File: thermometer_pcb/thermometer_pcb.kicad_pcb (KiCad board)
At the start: 2 copper layers, 76.6 x 49 mm, 23 parts, among them J1 POWER_IN, J2 TC_IN, J3 EXT_DS1, J4 EXT_DS2, J5 DISP, J6 Conn_01x02, J7 SPI, J8 I2C, J9 ENC, Q1 PN2222A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

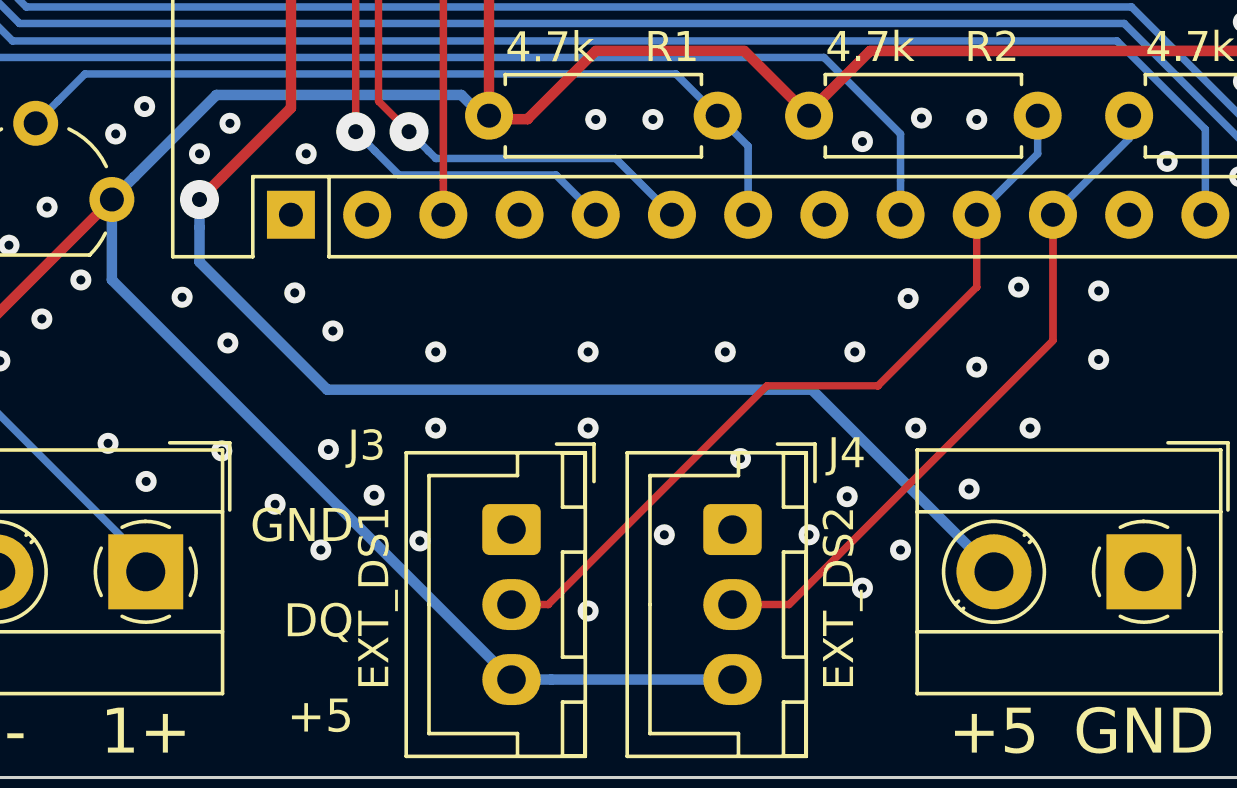
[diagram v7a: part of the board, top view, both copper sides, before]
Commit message: pcb: get rid of via on Vin track
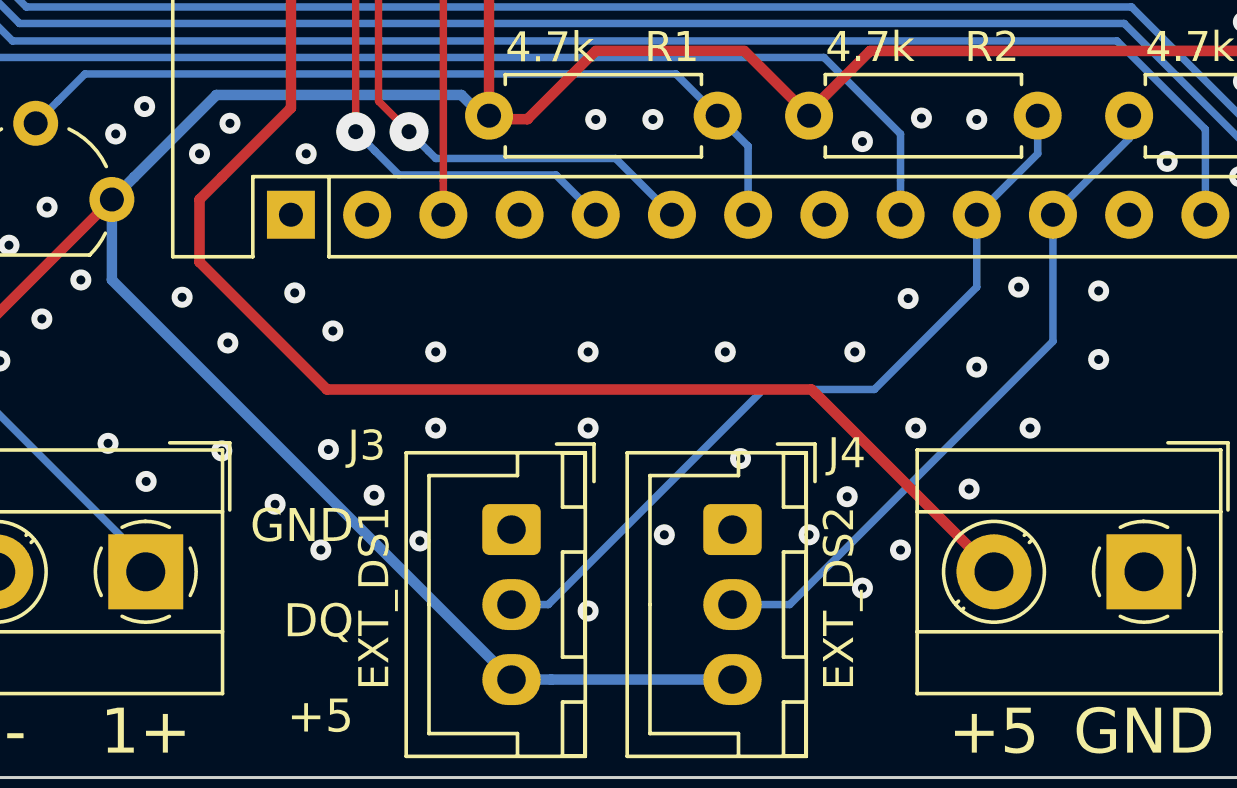
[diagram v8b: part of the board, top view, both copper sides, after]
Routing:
- net /Vin: vias 1 -> 0
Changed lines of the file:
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@@
   (gr_line (start 222.221676 76.190177) (end 222.221676 46.018604) (layer "Edge.Cuts") (width 0.1))
   (gr_arc (start 220.221676 46.018604) (end 222.221676 46.018604) (angle -90) (layer "Edge.Cuts") (width 0.1))
+  (segment (start 202.155677 80.082604) (end 205.568677 76.669604) (width 0.25) (layer "B.Cu") (net 20))
+  (segment (start 205.568677 76.669604) (end 205.568677 74.258604) (width 0.25) (layer "B.Cu") (net 20))
+  (segment (start 198.455677 80.082604) (end 202.155677 80.082604) (width 0.25) (layer "B.Cu") (net 20))
+  (segment (start 190.060677 87.252604) (end 191.285677 87.252604) (width 0.25) (layer "B.Cu") (net 20))
+  (segment (start 191.285677 87.252604) (end 198.455677 80.082604) (width 0.25) (layer "B.Cu") (net 20))
+  (segment (start 199.335677 87.252604) (end 208.108677 78.479604) (width 0.25) (layer "B.Cu") (net 9))
+  (segment (start 208.108677 78.479604) (end 208.108677 74.258604) (width 0.25) (layer "B.Cu") (net 9))
+  (segment (start 197.426677 87.252604) (end 199.335677 87.252604) (width 0.25) (layer "B.Cu") (net 9))
+  (segment (start 183.905677 80.082604) (end 179.660681 75.837608) (width 0.35) (layer "F.Cu") (net 5))
+  (segment (start 179.660681 75.837608) (end 179.660681 73.750604) (width 0.35) (layer "F.Cu") (net 5))
+  (segment (start 200.055677 80.082604) (end 183.905677 80.082604) (width 0.35) (layer "F.Cu") (net 5))
+  (segment (start 200.205677 80.232604) (end 200.055677 80.082604) (width 0.35) (layer "F.Cu") (net 5))
+  (segment (start 200.214677 80.232604) (end 200.205677 80.232604) (width 0.35) (layer "F.Cu") (net 5))
+  (segment (start 206.142677 86.160604) (end 200.214677 80.232604) (width 0.35) (layer "F.Cu") (net 5))
   (via micro (at 214.331677 72.988604) (size 0.7) (drill 0.3) (layers "F.Cu" "B.Cu") (net 1))
   (segment (start 191.385677 89.752604) (end 197.426677 89.752604) (width 0.35) (layer "B.Cu") (net 2))
@@
   (segment (start 208.123877 74.243404) (end 208.108677 74.258604) (width 0.25) (layer "B.Cu") (net 9))
   (segment (start 205.583877 74.243404) (end 205.568677 74.258604) (width 0.25) (layer "F.Cu") (net 20))
-  (segment (start 208.108677 78.454204) (end 208.108677 74.258604) (width 0.25) (layer "F.Cu") (net 9))
-  (segment (start 197.426677 87.252604) (end 199.310277 87.252604) (width 0.25) (layer "F.Cu") (net 9))
-  (segment (start 199.310277 87.252604) (end 208.108677 78.454204) (width 0.25) (layer "F.Cu") (net 9))
   (segment (start 210.648677 71.718604) (end 210.648677 70.956604) (width 0.25) (layer "B.Cu") (net 9))
   (segment (start 208.108677 74.258604) (end 210.648677 71.718604) (width 0.25) (layer "B.Cu") (net 9))
   (segment (start 207.600677 72.226604) (end 207.600677 70.956604) (width 0.25) (layer "B.Cu") (net 20))
   (segment (start 205.568677 74.258604) (end 207.600677 72.226604) (width 0.25) (layer "B.Cu") (net 20))
-  (segment (start 205.568677 76.671604) (end 205.568677 74.258604) (width 0.25) (layer "F.Cu") (net 20))
-  (segment (start 202.277277 79.963004) (end 205.568677 76.671604) (width 0.25) (layer "F.Cu") (net 20))
-  (segment (start 190.060677 87.252604) (end 191.285677 87.252604) (width 0.25) (layer "F.Cu") (net 20))
-  (segment (start 198.575277 79.963004) (end 202.277277 79.963004) (width 0.25) (layer "F.Cu") (net 20))
-  (segment (start 191.285677 87.252604) (end 198.575277 79.963004) (width 0.25) (layer "F.Cu") (net 20))
   (segment (start 197.948677 71.972604) (end 196.932677 70.956604) (width 0.25) (layer "B.Cu") (net 12))
   (segment (start 197.948677 74.258604) (end 197.948677 71.972604) (width 0.25) (layer "B.Cu") (net 12))
@@
   (segment (start 189.312677 70.956604) (end 189.312677 61.626704) (width 0.35) (layer "F.Cu") (net 2))
   (segment (start 189.312677 61.626704) (end 190.328677 60.610704) (width 0.35) (layer "F.Cu") (net 2))
-  (via (at 179.660681 73.750604) (size 1.3) (drill 0.5) (layers "F.Cu" "B.Cu") (net 5))
   (segment (start 187.788677 73.127234) (end 187.788677 59.018604) (width 0.25) (layer "F.Cu") (net 8) (status 40000))
   (segment (start 187.788677 74.258604) (end 187.788677 73.127234) (width 0.25) (layer "F.Cu") (net 8))
@@
   (via micro (at 183.957677 82.084604) (size 0.7) (drill 0.3) (layers "F.Cu" "B.Cu") (net 1))
   (segment (start 190.060677 89.752604) (end 176.739677 76.431604) (width 0.35) (layer "B.Cu") (net 2))
-  (segment (start 179.660681 74.669842) (end 179.660681 73.750604) (width 0.35) (layer "B.Cu") (net 5))
-  (segment (start 179.660681 75.831526) (end 179.660681 74.669842) (width 0.35) (layer "B.Cu") (net 5))
   (via micro (at 184.105677 78.132604) (size 0.7) (drill 0.3) (layers "F.Cu" "B.Cu") (net 1))
   (via micro (at 182.835677 76.862604) (size 0.7) (drill 0.3) (layers "F.Cu" "B.Cu") (net 1))
-  (segment (start 200.072077 80.090004) (end 183.919159 80.090004) (width 0.35) (layer "B.Cu") (net 5))
-  (segment (start 206.142677 86.160604) (end 200.072077 80.090004) (width 0.35) (layer "B.Cu") (net 5))
-  (segment (start 183.919159 80.090004) (end 179.660681 75.831526) (width 0.35) (layer "B.Cu") (net 5))
   (segment (start 165.636477 54.954604) (end 167.492777 56.810904) (width 0.25) (layer "F.Cu") (net 4))
   (segment (start 157.510577 52.772304) (end 159.692877 54.954604) (width 0.25) (layer "F.Cu") (net 4))
